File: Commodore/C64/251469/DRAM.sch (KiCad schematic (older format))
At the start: 16 parts, among them U10 4164, U11 4164, U12 4164, U21 4164, U22 4164, U23 4164, U24 4164, U9 4164

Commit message: WIP
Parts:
- added R? (x8): 33Ω, symbol Device:R
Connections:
- net ~RAS is gone; now on net R~W: U10.4 (~RAS), U11.4 (~RAS), U12.4 (~RAS), U21.4 (~RAS), U22.4 (~RAS), U23.4 (~RAS), U24.4 (~RAS), U9.4 (~RAS)
- net MA0: now also R?.2; no longer U10.5 (A0), U11.5 (A0), U12.5 (A0), U21.5 (A0), U22.5 (A0), U23.5 (A0), U24.5 (A0), U9.5 (A0)
- net MA1: now also R?.2; no longer U10.7 (A1), U11.7 (A1), U12.7 (A1), U21.7 (A1), U22.7 (A1), U23.7 (A1), U24.7 (A1), U9.7 (A1)
- net MA2: now also R?.2; no longer U10.6 (A2), U11.6 (A2), U12.6 (A2), U21.6 (A2), U22.6 (A2), U23.6 (A2), U24.6 (A2), U9.6 (A2)
- net MA3: now also R?.2; no longer U10.12 (A3), U11.12 (A3), U12.12 (A3), U21.12 (A3), U22.12 (A3), U23.12 (A3), U24.12 (A3), U9.12 (A3)
- net MA4: now also R?.2; no longer U10.11 (A4), U11.11 (A4), U12.11 (A4), U21.11 (A4), U22.11 (A4), U23.11 (A4), U24.11 (A4), U9.11 (A4)
- net MA5: now also R?.2; no longer U10.10 (A5), U11.10 (A5), U12.10 (A5), U21.10 (A5), U22.10 (A5), U23.10 (A5), U24.10 (A5), U9.10 (A5)
- net MA6: now also R?.2; no longer U10.13 (A6), U11.13 (A6), U12.13 (A6), U21.13 (A6), U22.13 (A6), U23.13 (A6), U24.13 (A6), U9.13 (A6)
- net MA7: now also R?.2; no longer U10.9 (A7), U11.9 (A7), U12.9 (A7), U21.9 (A7), U22.9 (A7), U23.9 (A7), U24.9 (A7), U9.9 (A7)
- new net MA'0: R?.1, U10.5 (A0), U11.5 (A0), U12.5 (A0), U21.5 (A0), U22.5 (A0), U23.5 (A0), U24.5 (A0), U9.5 (A0)
- new net MA'1: R?.1, U10.7 (A1), U11.7 (A1), U12.7 (A1), U21.7 (A1), U22.7 (A1), U23.7 (A1), U24.7 (A1), U9.7 (A1)
- new net MA'2: R?.1, U10.6 (A2), U11.6 (A2), U12.6 (A2), U21.6 (A2), U22.6 (A2), U23.6 (A2), U24.6 (A2), U9.6 (A2)
- new net MA'3: R?.1, U10.12 (A3), U11.12 (A3), U12.12 (A3), U21.12 (A3), U22.12 (A3), U23.12 (A3), U24.12 (A3), U9.12 (A3)
- new net MA'4: R?.1, U10.11 (A4), U11.11 (A4), U12.11 (A4), U21.11 (A4), U22.11 (A4), U23.11 (A4), U24.11 (A4), U9.11 (A4)
- new net MA'5: R?.1, U10.10 (A5), U11.10 (A5), U12.10 (A5), U21.10 (A5), U22.10 (A5), U23.10 (A5), U24.10 (A5), U9.10 (A5)
- new net MA'6: R?.1, U10.13 (A6), U11.13 (A6), U12.13 (A6), U21.13 (A6), U22.13 (A6), U23.13 (A6), U24.13 (A6), U9.13 (A6)
- new net MA'7: R?.1, U10.9 (A7), U11.9 (A7), U12.9 (A7), U21.9 (A7), U22.9 (A7), U23.9 (A7), U24.9 (A7), U9.9 (A7)
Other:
- moved on the sheet: C25, C26, C27, C28, C40, C41, C42, C43, U10, U11, U12, U21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

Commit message: WIP
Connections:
- net R~W: no longer U10.4 (~RAS), U11.4 (~RAS), U12.4 (~RAS), U21.4 (~RAS), U22.4 (~RAS), U23.4 (~RAS), U24.4 (~RAS), U9.4 (~RAS)
- new net ~RAS: U10.4 (~RAS), U11.4 (~RAS), U12.4 (~RAS), U21.4 (~RAS), U22.4 (~RAS), U23.4 (~RAS), U24.4 (~RAS), U9.4 (~RAS)
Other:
- moved on the sheet: C25, C26, C27, C28, C40, C41, C42, C43, R?, U10, U11, U12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

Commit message: WIP
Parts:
- removed R? (x8): 33Ω, symbol Device:R
- added RP1, RP2: 33R, Resistor_THT:R_Array_SIP8, symbol Device:R_Pack04_SIP
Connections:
- net MA'0: now also RP2.4 (R2.2)
- net MA'1: now also RP2.8 (R4.2)
- net MA'2: now also RP2.6 (R3.2)
- net MA'3: now also RP2.2 (R1.2)
- net MA'4: now also RP1.4 (R2.2)
- net MA'5: now also RP1.6 (R3.2)
- net MA'6: now also RP1.2 (R1.2)
- net MA'7: now also RP1.8 (R4.2)
- net MA0: now also RP2.3 (R2.1)
- net MA1: now also RP2.7 (R4.1)
- net MA2: now also RP2.5 (R3.1)
- net MA3: now also RP2.1 (R1.1)
- net MA4: now also RP1.3 (R2.1)
- net MA5: now also RP1.5 (R3.1)
- net MA6: now also RP1.1 (R1.1)
- net MA7: now also RP1.7 (R4.1)
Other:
- moved on the sheet: C25, C26, C27, C28, C40, C41, C42, C43, U10, U11, U12, U21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

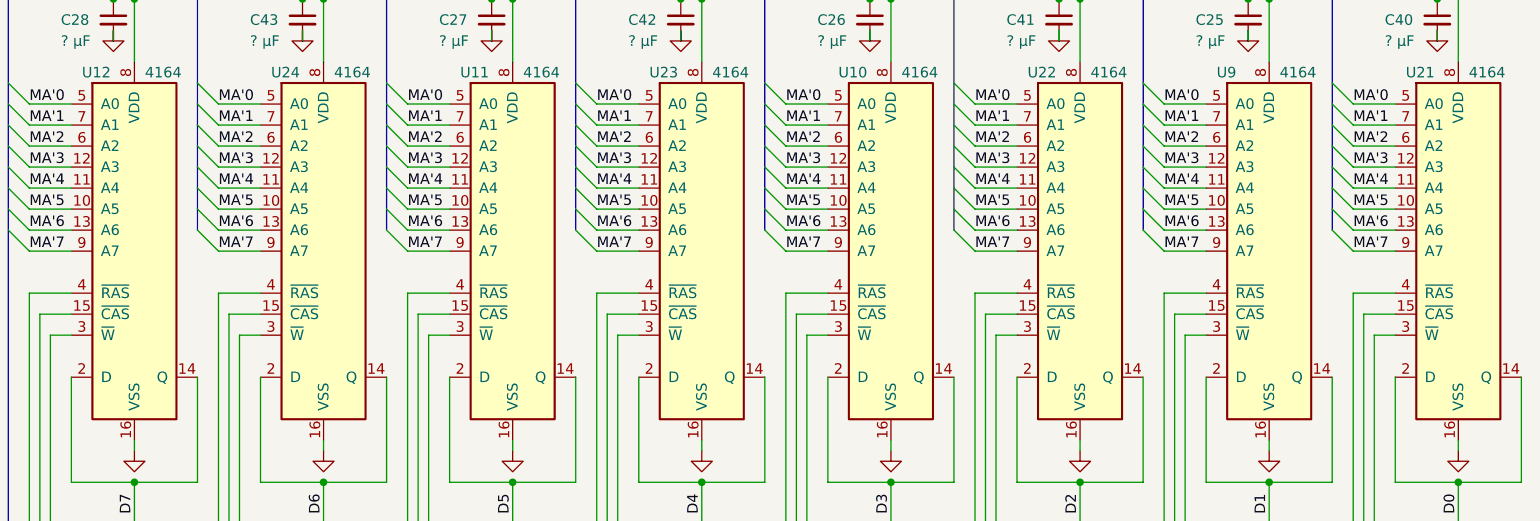
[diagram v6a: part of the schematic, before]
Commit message: Power section skeleton
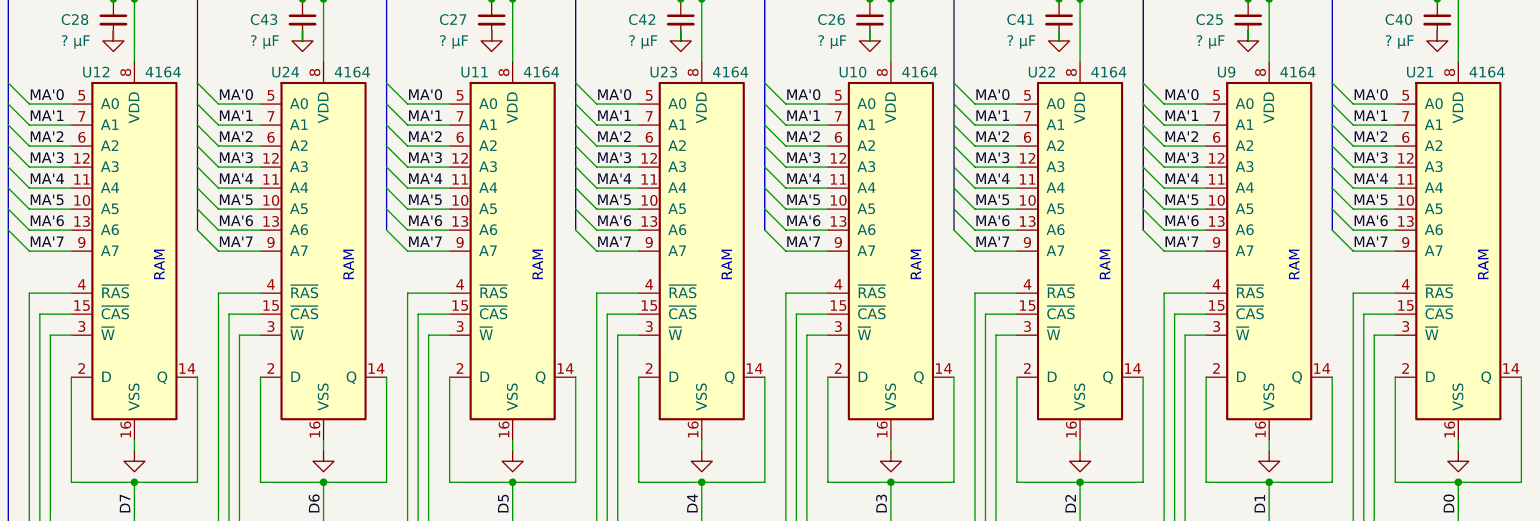
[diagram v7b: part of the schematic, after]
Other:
- note added: "RAM"
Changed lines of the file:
@@
 $Descr A4 11693 8268
 encoding utf-8
-Sheet 5 6
+Sheet 5 7
 Title "Commodore 64 - DRAM Section (schematic #251469)"
 Date "2019-07-11"
@@
 	0    -1   -1   0
 $EndComp
+Text Notes 3100 2100 1    50   ~ 0
+RAM
+Text Notes 4000 2100 1    50   ~ 0
+RAM
+Text Notes 4900 2100 1    50   ~ 0
+RAM
+Text Notes 5800 2100 1    50   ~ 0
+RAM
+Text Notes 6700 2100 1    50   ~ 0
+RAM
+Text Notes 7600 2100 1    50   ~ 0
+RAM
+Text Notes 8500 2100 1    50   ~ 0
+RAM
+Text Notes 9400 2100 1    50   ~ 0
+RAM
 Wire Bus Line
 	1400 1100 1400 3250
